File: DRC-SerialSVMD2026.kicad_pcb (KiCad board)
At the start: 2 copper layers, 80 x 60 mm, 67 parts, among them J1 CAN, J10 BATT, J11 SerialServo1, J12 SerialServo2, J13 SerialServo3, J14 SerialServo4, J15 USB_C, J2 CAN, J3 STLINK, J4 SW1, J5 SW2, J6 SW3, J7 SW4, J8 SW5, J9 SW6, Q1 2PB709AR, SW1 DIP, SW2 SW_Push, SW3 SSSS213202, U1 RT9080-33GJ5, U2 STM32F303K8Tx, U3 ADuM121N, U4 MAX485E, U5 CH340E, U6 BP5293-50

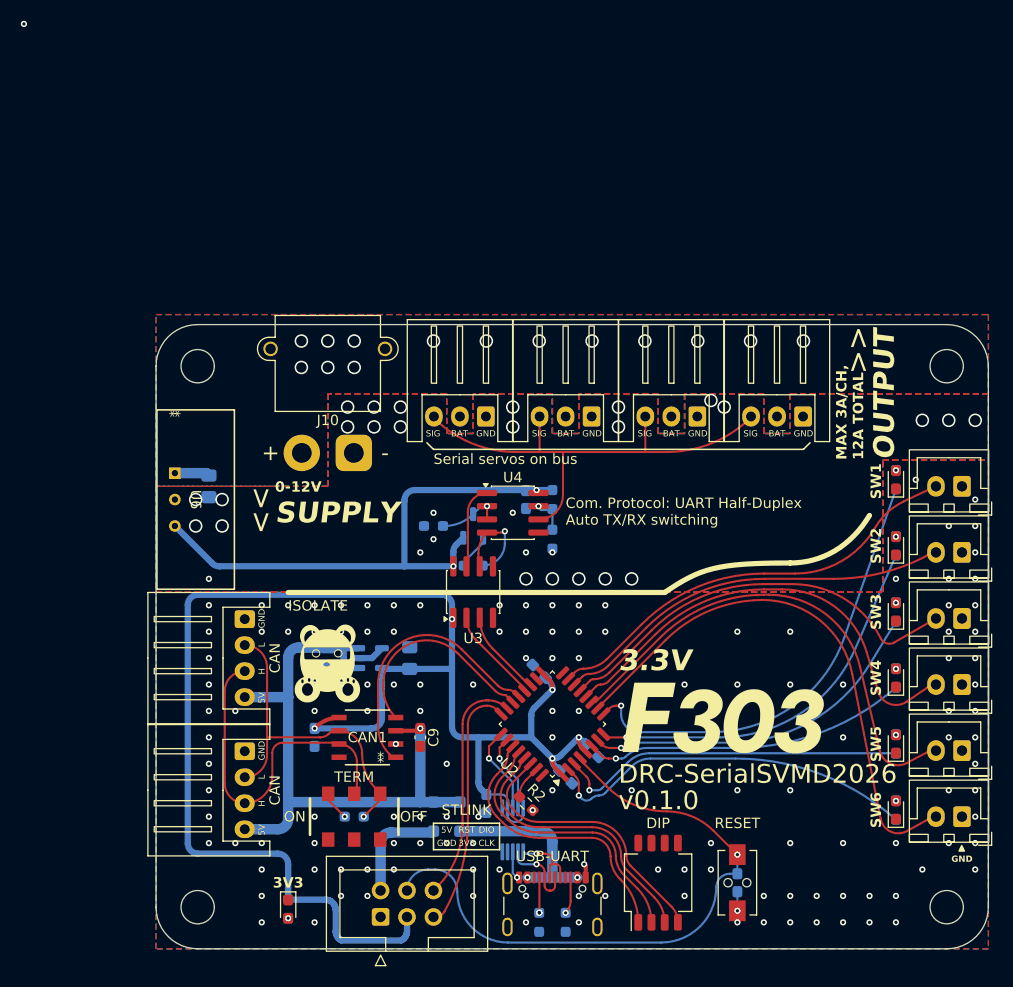
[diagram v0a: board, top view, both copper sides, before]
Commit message: サーボと直接シリアル通信するためのUSB端子を追加、v0.1.1
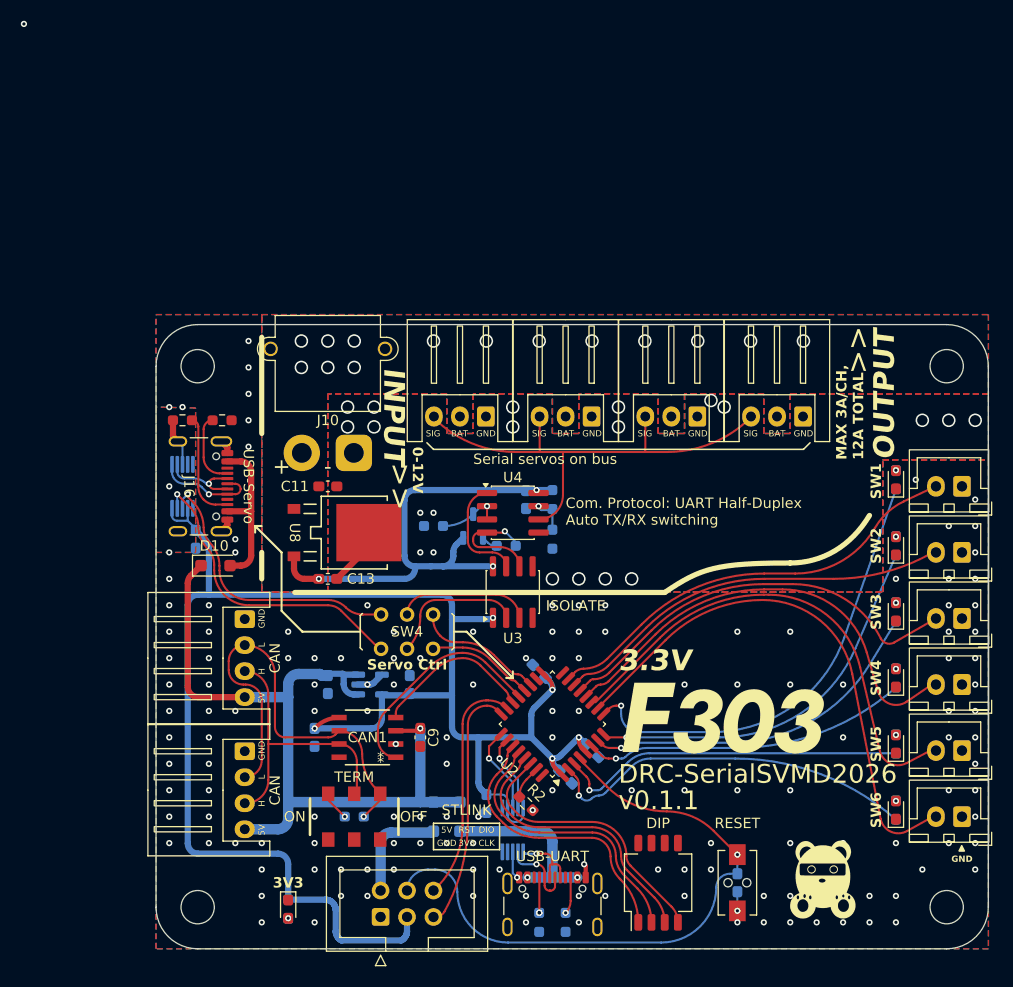
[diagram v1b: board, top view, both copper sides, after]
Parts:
- removed U6: BP5293-50, lib:SIP03_BP5293_17X7P2_ROM
- added C12: 0.1u, Capacitor_SMD:C_0603_1608Metric_Pad1.08x0.95mm_HandSolder, B.Cu at (113.8, 90.6)
- added C13: 0.1u, Capacitor_SMD:C_0603_1608Metric_Pad1.08x0.95mm_HandSolder, F.Cu at (126.5, 94.4)
- added D10: SS2040FL, Diode_SMD:D_SOD-123F, F.Cu at (115.7, 93.2)
- added J16: USB_C, Connector_USB:USB_C_Receptacle_GCT_USB4105-xx-A_16P_TopMnt_Horizontal, F.Cu at (113.2, 85.5)
- added R16: 5.1k, Resistor_SMD:R_0603_1608Metric_Pad0.98x0.95mm_HandSolder, F.Cu at (116.3, 79.2)
- added R17: 5.1k, Resistor_SMD:R_0603_1608Metric_Pad0.98x0.95mm_HandSolder, F.Cu at (112.5, 79.2)
- added SW4: SWCTL, lib:IS-2235, F.Cu at (134.1, 99.5)
- added U7: CH340E, Package_SO:MSOP-10_3x3mm_P0.5mm, B.Cu at (112.5, 85.5)
- added U8: NJM7805SDL1-TE1, lib:TO-252-3-L1_NMD, F.Cu at (129.1, 90.0)
- C1, C2: footprint Capacitor_SMD:C_0805_2012Metric_Pad1.18x1.45mm_HandSolder -> Capacitor_SMD:C_0603_1608Metric_Pad1.08x0.95mm_HandSolder
- C11: value 10u -> 1u; footprint Capacitor_SMD:C_0805_2012Metric_Pad1.18x1.45mm_HandSolder -> Capacitor_SMD:C_0603_1608Metric_Pad1.08x0.95mm_HandSolder; moved to F.Cu
- moved G*** 52.0 mm to (174.1, 123.5)
- moved C11 11.4 mm to (126.5, 85.5), turned to 0 degrees
- moved U3 3.81 mm to (144.3, 95.7)
- moved R3 3.70 mm to (143.7, 91.3)
- moved C1 2.54 mm to (126.5, 104.6)
- moved C2 2.54 mm to (134.4, 104.6)
- moved U1 2.54 mm to (130.6, 104.6)
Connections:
- U3 pad 2: /MCU/USART_SSV_RX -> /SerialServoDrive/RXIN
- U3 pad 3: /MCU/USART_SSV_TX -> /SerialServoDrive/TXIN
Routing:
- net /USB_Servo/UART_RX: track 0.00 -> 29.2 mm, vias 0 -> 1
- net /USB_Servo/UART_TX: track 0.00 -> 27.1 mm, vias 0 -> 1
- net +5V: track 59.8 -> 76.2 mm
- net Net-(D10-A): track 0.00 -> 15.7 mm
- net /SerialServoDrive/RXIN: track 0.00 -> 13.5 mm
- net +3V3: track 154.3 -> 167.3 mm
- net /SerialServoDrive/TXIN: track 0.00 -> 13.0 mm
- net Net-(J16-CC2): track 0.00 -> 10.5 mm
- net /USB_Servo/USB_D_P: track 0.00 -> 10.1 mm, vias 0 -> 1
- net /CAN/CAN_L: track 32.1 -> 42.0 mm
- net /USB_Servo/USB_D_N: track 0.00 -> 8.29 mm, vias 0 -> 1
- net GND: track 9.41 -> 16.7 mm, vias 143 -> 156
- net Net-(J16-CC1): track 0.00 -> 7.12 mm
- net /CAN/CAN_H: track 33.6 -> 27.6 mm
- net GNDPWR: track 0.00 -> 5.72 mm, vias 31 -> 21
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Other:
- board text added: "INPUT"
- board text added: "Servo Ctrl"
- board text added: "USB-Servo"
- board text added: "v0.1.1"
- board text removed: "SUPPLY"
- board text removed: "v0.1.0"

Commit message: isolate のシルクを修正
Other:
- board text added: "v0.1.2"
- board text removed: "v0.1.1"
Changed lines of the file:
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@@
 	)
 	(gr_line
-		(start 111.27 95.71)
+		(start 120.16 94.71)
+		(end 120.16 75.39)
+		(stroke
+			(width 0.5)
+			(type solid)
+		)
+		(layer "B.SilkS")
+	)
+	(gr_arc
+		(start 121.16 95.71)
+		(mid 120.452893 95.417107)
+		(end 120.16 94.71)
+		(stroke
+			(width 0.5)
+			(type default)
+		)
+		(layer "B.SilkS")
+	)
+	(gr_line
+		(start 121.16 95.71)
 		(end 176.04 95.71)
 		(stroke
@@
 		)
 	)
-	(gr_text "v0.1.1"
+	(gr_text "v0.1.2"
 		(at 154.45 116.801521 0)
 		(layer "F.SilkS")
@@
 			(justify left bottom)
 		)
-		(render_cache "v0.1.1" 0
+		(render_cache "v0.1.2" 0
 			(polygon
 				(pts
@@
 			(polygon
 				(pts
-					(xy 161.043787 116.572897) (xy 161.062246 116.569376) (xy 161.075188 116.558803) (xy 161.081596 116.535198)
-					(xy 161.081596 116.404076) (xy 161.077502 116.376063) (xy 161.067778 116.366193) (xy 161.048843 116.361321)
-					(xy 160.920151 116.346401) (xy 160.884919 116.333258) (xy 160.863815 116.313293) (xy 160.85024 116.267752)
-					(xy 160.847159 116.225034) (xy 160.841581 116.074226) (xy 160.839685 115.995543) (xy 160.843687 115.403909)
-					(xy 160.857632 114.937645) (xy 160.869911 114.762141) (xy 160.872438 114.721805) (xy 160.868826 114.695728)
-					(xy 160.857606 114.682433) (xy 160.839685 114.67894) (xy 160.814406 114.681468) (xy 160.66992 114.703121)
-					(xy 160.547018 114.713916) (xy 160.4339 114.716749) (xy 160.38609 114.716749) (xy 160.371225 114.720461)
-					(xy 160.359976 114.732379) (xy 160.355865 114.75203) (xy 160.354642 114.822253) (xy 160.353337 114.898209)
-					(xy 160.358379 114.931869) (xy 160.368221 114.938889) (xy 160.38609 114.940964) (xy 160.521746 114.945864)
-					(xy 160.550411 114.953544) (xy 160.562461 114.966095) (xy 160.565022 114.986466) (xy 160.569968 115.301796)
-					(xy 160.559322 115.955931) (xy 160.547327 116.227562) (xy 160.537866 116.296223) (xy 160.52031 116.328555)
-					(xy 160.481821 116.343626) (xy 160.398352 116.355181) (xy 160.323112 116.358793) (xy 160.309462 116.366207)
-					(xy 160.29776 116.382644) (xy 160.295305 116.396602) (xy 160.297062 116.486465) (xy 160.297833 116.52003)
-					(xy 160.301445 116.548796) (xy 160.312665 116.566999) (xy 160.330586 116.572897) (xy 160.335642 116.572897)
-					(xy 160.696034 116.565423) (xy 161.038731 116.572897)
+					(xy 161.225247 116.078854) (xy 161.213371 116.060838) (xy 161.192494 116.053685) (xy 161.138031 116.052556)
+					(xy 161.066428 116.051157) (xy 161.043987 116.0546) (xy 161.030206 116.06463) (xy 161.021146 116.086438)
+					(xy 160.98615 116.228731) (xy 160.964403 116.273315) (xy 160.934153 116.30377) (xy 160.891146 116.322783)
+					(xy 160.83113 116.333039) (xy 160.643058 116.338021) (xy 160.499406 116.335602) (xy 160.483703 116.330231)
+					(xy 160.479293 116.322963) (xy 160.485534 116.31078) (xy 160.489405 116.305377) (xy 160.720982 116.028502)
+					(xy 160.894489 115.822781) (xy 160.975063 115.717507) (xy 161.051371 115.605695) (xy 161.100926 115.521605)
+					(xy 161.140708 115.440506) (xy 161.170596 115.364054) (xy 161.191852 115.290719) (xy 161.204695 115.221805)
+					(xy 161.209918 115.156133) (xy 161.21008 115.142647) (xy 161.206627 115.081719) (xy 161.196524 115.024427)
+					(xy 161.180067 114.970664) (xy 161.157677 114.920827) (xy 161.095412 114.832071) (xy 161.01085 114.75942)
+					(xy 160.90528 114.705438) (xy 160.781274 114.673676) (xy 160.683394 114.66663) (xy 160.548502 114.679091)
+					(xy 160.417571 114.71536) (xy 160.295494 114.771555) (xy 160.231062 114.809909) (xy 160.20463 114.825449)
+					(xy 160.180247 114.839502) (xy 160.167613 114.856529) (xy 160.164293 114.875897) (xy 160.166821 114.901067)
+					(xy 160.167921 114.908106) (xy 160.17556 114.968965) (xy 160.17946 115.079779) (xy 160.17946 115.130117)
+					(xy 160.182984 115.146882) (xy 160.193579 115.161728) (xy 160.217269 115.170344) (xy 160.323112 115.170344)
+					(xy 160.346979 115.156311) (xy 160.358393 115.140119) (xy 160.391579 115.069458) (xy 160.441638 114.998963)
+					(xy 160.475972 114.967868) (xy 160.518097 114.941724) (xy 160.569204 114.922167) (xy 160.630485 114.910833)
+					(xy 160.675811 114.90865) (xy 160.719466 114.912141) (xy 160.760446 114.922511) (xy 160.796994 114.939011)
+					(xy 160.829699 114.961705) (xy 160.857054 114.989403) (xy 160.879618 115.02263) (xy 160.896514 115.060431)
+					(xy 160.90769 115.103296) (xy 160.912775 115.162761) (xy 160.909165 115.215812) (xy 160.897959 115.273753)
+					(xy 160.878185 115.33737) (xy 160.849379 115.405345) (xy 160.80946 115.479849) (xy 160.66779 115.690782)
+					(xy 160.41785 116.015528) (xy 160.089512 116.40244) (xy 160.008112 116.491784) (xy 160.000528 116.511897)
+					(xy 160.012505 116.541969) (xy 160.051479 116.574056) (xy 160.073618 116.579931) (xy 160.076146 116.579931)
+					(xy 160.534687 116.569929) (xy 161.162159 116.579931) (xy 161.186413 116.564653) (xy 161.19744 116.529592)
+					(xy 161.195022 116.514425) (xy 161.189966 116.446391) (xy 161.200623 116.296481) (xy 161.212133 116.202749)
+					(xy 161.225247 116.081382)
 				)
 			)
@@
 	)
 	(group "MCU"
-		(members "1c1c0895-eb59-40dc-8827-710e1f8367ff" "267563e1-b735-4af6-afb0-c8b043d4830a"
-			"29b73ba1-c84a-461f-93ec-14679df263ba" "411497b0-2572-478d-9270-43dd2aee0477"
-			"4b38c7ae-3fbc-4715-a195-ac3e672ba9e9" "4c7d9420-bb02-4b3f-8202-d40dd3b2b0d0"
-			"9f8393af-8f09-4252-95af-34a7b79c215e" "a1fcd4c2-2f9b-49a3-8b6b-68583fd9755e"
-			"c6befce5-84a5-4a3a-a24d-d3f20b46ee20" "f2b7f10b-5e7b-48d9-8bca-f1c3a30363f0"
+		(members "1c1c0895-eb59-40dc-8827-710e1f8367ff" "4c7d9420-bb02-4b3f-8202-d40dd3b2b0d0"
+			"9f8393af-8f09-4252-95af-34a7b79c215e" "c6befce5-84a5-4a3a-a24d-d3f20b46ee20"
+			"f2b7f10b-5e7b-48d9-8bca-f1c3a30363f0"
 		)
 	)
